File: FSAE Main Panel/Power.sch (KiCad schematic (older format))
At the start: 9 parts, among them Q301 Q_PMOS_GSD, U302 LP2985-3.3

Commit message: Added power regulator for LEDs, further GPIO considerations
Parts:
- added C?: 10uF, symbol CP1
- added C?: 100uF, symbol CP1
- added U?: LM1085-5.0, symbol LM1085-5.0
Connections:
- net labels added: DWC_+5V, LED_+5V
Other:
- note added: "LED Power"
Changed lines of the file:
@@
 	8050 4600 8200 4600
 Wire Wire Line
-	8200 4450 8200 4600
-Wire Wire Line
-	8200 4600 8200 5050
+	8200 4450 8200 5050
 Wire Wire Line
 	8200 5850 8200 5350
@@
 	6400 5200 6400 4600
 Wire Wire Line
-	6400 4600 7000 4600
-Wire Wire Line
-	7000 4600 7250 4600
-Wire Wire Line
-	6200 4450 6200 4600
-Wire Wire Line
-	6200 4600 6200 5200
+	6400 4600 7250 4600
+Wire Wire Line
+	6200 4450 6200 5200
 Text Notes 600  850  0    60   ~ 0
 Peak total draw for low power LEDs is 1.2A at 5V\nPeak total draw for high power LEDs is \nPeak total draw for alarm cluster is 800mA at 5V
@@
 	6000 4600 6000 4900
 Wire Wire Line
-	3950 5850 4600 5850
-Wire Wire Line
-	4600 5850 5200 5850
-Wire Wire Line
-	5200 5850 6700 5850
-Wire Wire Line
-	6700 5850 7000 5850
-Wire Wire Line
-	7000 5850 7650 5850
-Wire Wire Line
-	7650 5850 8200 5850
+	3950 5850 8200 5850
 $Comp
 L GND #PWR302
@@
 $EndComp
 Wire Wire Line
-	5150 4600 5200 4600
-Wire Wire Line
-	5200 4600 6000 4600
-Wire Wire Line
-	6000 4600 6200 4600
+	5150 4600 6200 4600
 Wire Wire Line
 	4600 5050 4600 5850
@@
 $EndComp
 Wire Wire Line
-	3850 4600 3950 4600
-Wire Wire Line
-	3950 4600 4050 4600
+	3850 4600 4050 4600
 Wire Wire Line
 	3950 4600 3950 5050
@@
 	1    0    0    -1
 $EndComp
+$Comp
+L +12V #PWR?
+U 1 1 5C034AE4
+P 4250 2550
+F 0 "#PWR?" H 4250 2400 50  0001 C CNN
+F 1 "+12V" H 4250 2690 50  0000 C CNN
+F 2 "" H 4250 2550 50  0001 C CNN
+F 3 "" H 4250 2550 50  0001 C CNN
+	1    4250 2550
+	1    0    0    -1
+$EndComp
+$Comp
+L LM1085-5.0 U?
+U 1 1 5C0353B0
+P 5100 2750
+F 0 "U?" H 4950 2875 50  0000 C CNN
+F 1 "LM1085-5.0" H 5100 2875 50  0000 L CNN
+F 2 "" H 5100 3000 50  0001 C CIN
+F 3 "" H 5100 2750 50  0001 C CNN
+	1    5100 2750
+	1    0    0    -1
+$EndComp
+Wire Wire Line
+	4250 2550 4250 2750
+Wire Wire Line
+	4250 2750 4800 2750
+$Comp
+L GND #PWR?
+U 1 1 5C03578E
+P 5100 3350
+F 0 "#PWR?" H 5100 3100 50  0001 C CNN
+F 1 "GND" H 5100 3200 50  0000 C CNN
+F 2 "" H 5100 3350 50  0001 C CNN
+F 3 "" H 5100 3350 50  0001 C CNN
+	1    5100 3350
+	1    0    0    -1
+$EndComp
+Wire Wire Line
+	5100 3050 5100 3350
+$Comp
+L CP1 C?
+U 1 1 5C036676
+P 4550 3050
+F 0 "C?" H 4575 3150 50  0000 L CNN
+F 1 "10uF" H 4575 2950 50  0000 L CNN
+F 2 "" H 4550 3050 50  0001 C CNN
+F 3 "" H 4550 3050 50  0001 C CNN
+	1    4550 3050
+	1    0    0    -1
+$EndComp
+$Comp
+L CP1 C?
+U 1 1 5C0366B5
+P 5650 3050
+F 0 "C?" H 5675 3150 50  0000 L CNN
+F 1 "100uF" H 5675 2950 50  0000 L CNN
+F 2 "" H 5650 3050 50  0001 C CNN
+F 3 "" H 5650 3050 50  0001 C CNN
+	1    5650 3050
+	1    0    0    -1
+$EndComp
+Wire Wire Line
+	4550 2900 4550 2750
+Connection ~ 4550 2750
+Wire Wire Line
+	4550 3200 4550 3300
+Wire Wire Line
+	4550 3300 5650 3300
+Connection ~ 5100 3300
+Wire Wire Line
+	5650 2900 5650 2750
+Wire Wire Line
+	5400 2750 6000 2750
+Wire Wire Line
+	5650 3300 5650 3200
+Text GLabel 6000 2750 2    60   Input ~ 0
+LED_+5V
+Text GLabel 6000 2550 2    60   Input ~ 0
+DWC_+5V
+Connection ~ 5650 2750
+Wire Wire Line
+	6000 2550 5850 2550
+Wire Wire Line
+	5850 2550 5850 2750
+Connection ~ 5850 2750
+Wire Notes Line
+	4100 3600 4100 2250
+Wire Notes Line
+	4100 2250 6550 2250
+Wire Notes Line
+	6550 2250 6550 3600
+Wire Notes Line
+	6550 3600 4100 3600
+Text Notes 5050 2400 0    60   ~ 0
+LED Power
 $EndSCHEMATC

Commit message: Updated to KiCad 5
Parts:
- C301, C303: renamed from C?; symbol C -> Device:C
- C302, C306: renamed from C?; symbol CP1 -> Device:CP1
- C304, C305: symbol C -> Device:C
- D301: symbol D -> Device:D
- L301: symbol Ferrite_Bead -> Device:Ferrite_Bead
- Q301: symbol Q_PMOS_GSD -> Device:Q_PMOS_GSD
- U301: renamed from U?; symbol ZLDO1117-5V -> zldo1117-5v:ZLDO1117-5V
- U302: symbol LP2985-3.3 -> regul:LP2985-3.3
- U303: renamed from U?; symbol LM1085-5.0 -> regul:LM1085-5.0
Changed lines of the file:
@@
-EESchema Schematic File Version 2
-LIBS:power
-LIBS:device
-LIBS:switches
-LIBS:relays
-LIBS:motors
-LIBS:transistors
-LIBS:conn
-LIBS:linear
-LIBS:regul
-LIBS:74xx
-LIBS:cmos4000
-LIBS:adc-dac
-LIBS:memory
-LIBS:xilinx
-LIBS:microcontrollers
-LIBS:dsp
-LIBS:microchip
-LIBS:analog_switches
-LIBS:motorola
-LIBS:texas
-LIBS:intel
-LIBS:audio
-LIBS:interface
-LIBS:digital-audio
-LIBS:philips
-LIBS:display
-LIBS:cypress
-LIBS:siliconi
-LIBS:opto
-LIBS:atmel
-LIBS:contrib
-LIBS:valves
-LIBS:TI_Additions
-LIBS:KingBright_Addition
-LIBS:lm2734
-LIBS:prtr5v0u2x
-LIBS:samd21g18a-au
-LIBS:zldo1117-5v
-LIBS:cortex_debug
+EESchema Schematic File Version 4
 LIBS:FSAE Main Panel-cache
-EELAYER 25 0
+EELAYER 26 0
 EELAYER END
 $Descr A4 11693 8268
@@
 $EndDescr
 $Comp
-L +12V #PWR301
+L power:+12V #PWR301
 U 1 1 5BD92350
 P 2800 4100
@@
 $EndComp
 $Comp
-L D D301
+L Device:D D301
 U 1 1 5BD92356
 P 3100 4600
@@
 $EndComp
 $Comp
-L Ferrite_Bead L301
+L Device:Ferrite_Bead L301
 U 1 1 5BD9235D
 P 3700 4600
@@
 $EndComp
 $Comp
-L +5V #PWR303
+L power:+5V #PWR304
 U 1 1 5BD923A9
 P 6200 4450
-F 0 "#PWR303" H 6200 4300 50  0001 C CNN
+F 0 "#PWR304" H 6200 4300 50  0001 C CNN
 F 1 "+5V" H 6200 4590 50  0000 C CNN
 F 2 "" H 6200 4450 50  0001 C CNN
@@
 $EndComp
 $Comp
-L LP2985-3.3 U302
+L regul:LP2985-3.3 U302
 U 1 1 5BD923AF
 P 7650 4700
@@
 $EndComp
 $Comp
-L C C304
+L Device:C C304
 U 1 1 5BD923BD
 P 7000 5200
@@
 	7000 5850 7000 5350
 $Comp
-L C C305
+L Device:C C305
 U 1 1 5BD92405
 P 8200 5200
@@
 Connection ~ 7650 5850
 $Comp
-L +3V3 #PWR304
+L power:+3V3 #PWR306
 U 1 1 5BD92411
 P 8200 4450
-F 0 "#PWR304" H 8200 4300 50  0001 C CNN
+F 0 "#PWR306" H 8200 4300 50  0001 C CNN
 F 1 "+3V3" H 8200 4590 50  0000 C CNN
 F 2 "" H 8200 4450 50  0001 C CNN
@@
 Connection ~ 8200 4600
 $Comp
-L Q_PMOS_GSD Q301
+L Device:Q_PMOS_GSD Q301
 U 1 1 5BD96D6D
 P 6000 5100
@@
 	3950 5850 8200 5850
 $Comp
-L GND #PWR302
+L power:GND #PWR305
 U 1 1 5BD92372
 P 6700 5950
-F 0 "#PWR302" H 6700 5700 50  0001 C CNN
+F 0 "#PWR305" H 6700 5700 50  0001 C CNN
 F 1 "GND" H 6700 5800 50  0000 C CNN
 F 2 "" H 6700 5950 50  0001 C CNN
@@
 Connection ~ 6700 5850
 $Comp
-L C C?
+L Device:C C301
 U 1 1 5BFABDFE
 P 3950 5200
-F 0 "C?" H 3975 5300 50  0000 L CNN
+F 0 "C301" H 3975 5300 50  0000 L CNN
 F 1 "4.7uF" H 3975 5100 50  0000 L CNN
 F 2 "" H 3988 5050 50  0001 C CNN
@@
 Connection ~ 3950 4600
 $Comp
-L C C?
+L Device:C C303
 U 1 1 5BFAC037
 P 5200 5200
-F 0 "C?" H 5225 5300 50  0000 L CNN
+F 0 "C303" H 5225 5300 50  0000 L CNN
 F 1 "4.7uF" H 5225 5100 50  0000 L CNN
 F 2 "" H 5238 5050 50  0001 C CNN
@@
 MCU Power
 $Comp
-L ZLDO1117-5V U?
+L zldo1117-5v:ZLDO1117-5V U301
 U 1 1 5BFDDF95
 P 4600 4600
-F 0 "U?" H 4700 4300 60  0000 C CNN
+F 0 "U301" H 4700 4300 60  0000 C CNN
 F 1 "ZLDO1117-5V" H 4600 4800 60  0000 C CNN
 F 2 "" H 4600 4600 60  0001 C CNN
@@
 $EndComp
 $Comp
-L +12V #PWR?
+L power:+12V #PWR302
 U 1 1 5C034AE4
 P 4250 2550
-F 0 "#PWR?" H 4250 2400 50  0001 C CNN
+F 0 "#PWR302" H 4250 2400 50  0001 C CNN
 F 1 "+12V" H 4250 2690 50  0000 C CNN
 F 2 "" H 4250 2550 50  0001 C CNN
@@
 $EndComp
 $Comp
-L LM1085-5.0 U?
+L regul:LM1085-5.0 U303
 U 1 1 5C0353B0
 P 5100 2750
-F 0 "U?" H 4950 2875 50  0000 C CNN
+F 0 "U303" H 4950 2875 50  0000 C CNN
 F 1 "LM1085-5.0" H 5100 2875 50  0000 L CNN
 F 2 "" H 5100 3000 50  0001 C CIN
@@
 	4250 2750 4800 2750
 $Comp
-L GND #PWR?
+L power:GND #PWR303
 U 1 1 5C03578E
 P 5100 3350
-F 0 "#PWR?" H 5100 3100 50  0001 C CNN
+F 0 "#PWR303" H 5100 3100 50  0001 C CNN
 F 1 "GND" H 5100 3200 50  0000 C CNN
 F 2 "" H 5100 3350 50  0001 C CNN
@@
 	5100 3050 5100 3350
 $Comp
-L CP1 C?
+L Device:CP1 C302
 U 1 1 5C036676
 P 4550 3050
-F 0 "C?" H 4575 3150 50  0000 L CNN
+F 0 "C302" H 4575 3150 50  0000 L CNN
 F 1 "10uF" H 4575 2950 50  0000 L CNN
 F 2 "" H 4550 3050 50  0001 C CNN
@@
 $EndComp
 $Comp
-L CP1 C?
+L Device:CP1 C306
 U 1 1 5C0366B5
 P 5650 3050
-F 0 "C?" H 5675 3150 50  0000 L CNN
+F 0 "C306" H 5675 3150 50  0000 L CNN
 F 1 "100uF" H 5675 2950 50  0000 L CNN
 F 2 "" H 5650 3050 50  0001 C CNN

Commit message: Updated Footprint Association
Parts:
- C301: footprint (none) -> Capacitors_SMD:C_1206; Description (none) -> Ceramic 4.7uF 25V X5R 1206
- C302: footprint (none) -> Capacitors_SMD:C_1206; symbol Device:CP1 -> Device:C; Description (none) -> Ceramic 10uF 25V X5R 1206
- C303: footprint (none) -> Capacitors_SMD:C_1206; Description (none) -> Ceramic 4.7uF 10V X5R 1206
- C304: footprint (none) -> Capacitors_SMD:C_1206; Description (none) -> Ceramic 47uF 10V X5R 1206
- C305: footprint (none) -> Capacitors_SMD:C_1206; Description (none) -> 4.7uF 10V X5R 1206
- C306: footprint (none) -> Capacitors_Tantalum_SMD:CP_Tantalum_Case-D_EIA-7343-31_Reflow; Description (none) -> Tantalum 100uF 10V 2917
- D301: value D -> BYS10-45-E3/TR; footprint (none) -> Diodes_SMD:D_SMA; Description (none) -> Schottky Diode 45V 1.5A DO214AC
- L301: value Ferrite_Bead -> 742792310 Ferrite Bead; footprint (none) -> Inductors_SMD:L_1210; Description (none) -> 30 Ohm Ferrite Bead 1210
- Q301: value Q_PMOS_GSD -> IRLML6402TRPBF; footprint (none) -> TO_SOT_Packages_SMD:SOT-23; Description (none) -> P-Channel MOSFET SOT-23
- U301: footprint (none) -> TO_SOT_Packages_SMD:TO-252-2
- U303: footprint (none) -> TO_SOT_Packages_SMD:TO-263-3_TabPin2; Description (none) -> Linear Regulator 5V 3A TO263
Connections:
- wire segments 35 -> 51
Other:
- note added: "Gate - 3\nSource - 2\nDrain - 1"
- moved on the sheet: D301, L301
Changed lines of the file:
@@
 $EndDescr
 $Comp
-L power:+12V #PWR301
+L power:+12V #PWR0301
 U 1 1 5BD92350
 P 2800 4100
-F 0 "#PWR301" H 2800 3950 50  0001 C CNN
+F 0 "#PWR0301" H 2800 3950 50  0001 C CNN
 F 1 "+12V" H 2800 4240 50  0000 C CNN
 F 2 "" H 2800 4100 50  0001 C CNN
@@
 L Device:D D301
 U 1 1 5BD92356
-P 3100 4600
-F 0 "D301" H 3100 4700 50  0000 C CNN
-F 1 "D" H 3100 4500 50  0000 C CNN
-F 2 "" H 3100 4600 50  0001 C CNN
-F 3 "" H 3100 4600 50  0001 C CNN
-	1    3100 4600
-	-1   0    0    1
+P 3200 4600
+F 0 "D301" H 3200 4700 50  0000 C CNN
+F 1 "BYS10-45-E3/TR" H 3200 4500 39  0000 C CNN
+F 2 "Diodes_SMD:D_SMA" H 3200 4600 50  0001 C CNN
+F 3 "" H 3200 4600 50  0001 C CNN
+F 4 "Schottky Diode 45V 1.5A DO214AC" H 3200 4600 50  0001 C CNN "Description"
+	1    3200 4600
+	-1   0    0    -1
 $EndComp
 $Comp
 L Device:Ferrite_Bead L301
 U 1 1 5BD9235D
-P 3700 4600
-F 0 "L301" V 3550 4625 50  0000 C CNN
-F 1 "Ferrite_Bead" V 3850 4600 50  0000 C CNN
-F 2 "" V 3630 4600 50  0001 C CNN
-F 3 "" H 3700 4600 50  0001 C CNN
-	1    3700 4600
-	0    1    1    0
-$EndComp
-$Comp
-L power:+5V #PWR304
+P 3750 4600
+F 0 "L301" V 3600 4625 50  0000 C CNN
+F 1 "742792310 Ferrite Bead" V 3900 4600 39  0000 C CNN
+F 2 "Inductors_SMD:L_1210" V 3680 4600 50  0001 C CNN
+F 3 "" H 3750 4600 50  0001 C CNN
+F 4 "30 Ohm Ferrite Bead 1210" V 3750 4600 50  0001 C CNN "Description"
+	1    3750 4600
+	0    1    -1   0
+$EndComp
+$Comp
+L power:+5V #PWR0304
 U 1 1 5BD923A9
 P 6200 4450
-F 0 "#PWR304" H 6200 4300 50  0001 C CNN
+F 0 "#PWR0304" H 6200 4300 50  0001 C CNN
 F 1 "+5V" H 6200 4590 50  0000 C CNN
 F 2 "" H 6200 4450 50  0001 C CNN
@@
 F 0 "C304" H 7025 5300 50  0000 L CNN
 F 1 "47uF" H 7025 5100 50  0000 L CNN
-F 2 "" H 7038 5050 50  0001 C CNN
+F 2 "Capacitors_SMD:C_1206" H 7038 5050 50  0001 C CNN
 F 3 "" H 7000 5200 50  0001 C CNN
+F 4 "Ceramic 47uF 10V X5R 1206" H 7000 5200 50  0001 C CNN "Description"
 	1    7000 5200
 	1    0    0    -1
 $EndComp
 Wire Wire Line
-	2800 4600 2950 4600
-Wire Wire Line
-	3250 4600 3550 4600
+	3350 4600 3600 4600
 Connection ~ 7000 4600
 Wire Wire Line
@@
 F 0 "C305" H 8225 5300 50  0000 L CNN
 F 1 "4.7uF" H 8225 5100 50  0000 L CNN
-F 2 "" H 8238 5050 50  0001 C CNN
+F 2 "Capacitors_SMD:C_1206" H 8238 5050 50  0001 C CNN
 F 3 "" H 8200 5200 50  0001 C CNN
+F 4 "4.7uF 10V X5R 1206" H 8200 5200 50  0001 C CNN "Description"
 	1    8200 5200
 	1    0    0    -1
@@
 	8050 4600 8200 4600
 Wire Wire Line
-	8200 4450 8200 5050
+	8200 4450 8200 4600
 Wire Wire Line
 	8200 5850 8200 5350
 Connection ~ 7650 5850
 $Comp
-L power:+3V3 #PWR306
+L power:+3V3 #PWR0306
 U 1 1 5BD92411
 P 8200 4450
-F 0 "#PWR306" H 8200 4300 50  0001 C CNN
+F 0 "#PWR0306" H 8200 4300 50  0001 C CNN
 F 1 "+3V3" H 8200 4590 50  0000 C CNN
 F 2 "" H 8200 4450 50  0001 C CNN
@@
 P 6000 5100
 F 0 "Q301" H 6200 5150 50  0000 L CNN
-F 1 "Q_PMOS_GSD" H 6200 5050 50  0000 L CNN
-F 2 "" H 6200 5200 50  0001 C CNN
+F 1 "IRLML6402TRPBF" H 6200 5050 39  0000 L CNN
+F 2 "TO_SOT_Packages_SMD:SOT-23" H 6200 5200 50  0001 C CNN
 F 3 "" H 6000 5100 50  0001 C CNN
+F 4 "P-Channel MOSFET SOT-23" H 6000 5100 50  0001 C CNN "Description"
 	1    6000 5100
-	0    1    1    0
+	0    -1   1    0
 $EndComp
 Text GLabel 5750 5200 0    39   Input ~ 0
@@
 	6400 5200 6400 4600
 Wire Wire Line
-	6400 4600 7250 4600
-Wire Wire Line
-	6200 4450 6200 5200
+	6400 4600 7000 4600
+Wire Wire Line
+	6200 4450 6200 4600
 Text Notes 600  850  0    60   ~ 0
 Peak total draw for low power LEDs is 1.2A at 5V\nPeak total draw for high power LEDs is \nPeak total draw for alarm cluster is 800mA at 5V
@@
 	6000 4600 6000 4900
 Wire Wire Line
-	3950 5850 8200 5850
-$Comp
-L power:GND #PWR305
+	3950 5850 4600 5850
+$Comp
+L power:GND #PWR0305
 U 1 1 5BD92372
 P 6700 5950
-F 0 "#PWR305" H 6700 5700 50  0001 C CNN
+F 0 "#PWR0305" H 6700 5700 50  0001 C CNN
 F 1 "GND" H 6700 5800 50  0000 C CNN
 F 2 "" H 6700 5950 50  0001 C CNN
@@
 $EndComp
 Wire Wire Line
-	5150 4600 6200 4600
+	5150 4600 5200 4600
 Wire Wire Line
 	4600 5050 4600 5850
@@
 F 0 "C301" H 3975 5300 50  0000 L CNN
 F 1 "4.7uF" H 3975 5100 50  0000 L CNN
-F 2 "" H 3988 5050 50  0001 C CNN
+F 2 "Capacitors_SMD:C_1206" H 3988 5050 50  0001 C CNN
 F 3 "" H 3950 5200 50  0001 C CNN
+F 4 "Ceramic 4.7uF 25V X5R 1206" H 3950 5200 50  0001 C CNN "Description"
 	1    3950 5200
 	1    0    0    -1
 $EndComp
 Wire Wire Line
-	3850 4600 4050 4600
+	3900 4600 3950 4600
 Wire Wire Line
 	3950 4600 3950 5050
@@
 F 0 "C303" H 5225 5300 50  0000 L CNN
 F 1 "4.7uF" H 5225 5100 50  0000 L CNN
-F 2 "" H 5238 5050 50  0001 C CNN
+F 2 "Capacitors_SMD:C_1206" H 5238 5050 50  0001 C CNN
 F 3 "" H 5200 5200 50  0001 C CNN
+F 4 "Ceramic 4.7uF 10V X5R 1206" H 5200 5200 50  0001 C CNN "Description"
 	1    5200 5200
 	1    0    0    -1
@@
 F 0 "U301" H 4700 4300 60  0000 C CNN
 F 1 "ZLDO1117-5V" H 4600 4800 60  0000 C CNN
-F 2 "" H 4600 4600 60  0001 C CNN
+F 2 "TO_SOT_Packages_SMD:TO-252-2" H 4600 4600 60  0001 C CNN
 F 3 "" H 4600 4600 60  0001 C CNN
 	1    4600 4600
@@
 $EndComp
 $Comp
-L power:+12V #PWR302
+L power:+12V #PWR0302
 U 1 1 5C034AE4
-P 4250 2550
-F 0 "#PWR302" H 4250 2400 50  0001 C CNN
-F 1 "+12V" H 4250 2690 50  0000 C CNN
-F 2 "" H 4250 2550 50  0001 C CNN
-F 3 "" H 4250 2550 50  0001 C CNN
-	1    4250 2550
+P 4150 2550
+F 0 "#PWR0302" H 4150 2400 50  0001 C CNN
+F 1 "+12V" H 4150 2690 50  0000 C CNN
+F 2 "" H 4150 2550 50  0001 C CNN
+F 3 "" H 4150 2550 50  0001 C CNN
+	1    4150 2550
 	1    0    0    -1
 $EndComp
@@
 F 0 "U303" H 4950 2875 50  0000 C CNN
 F 1 "LM1085-5.0" H 5100 2875 50  0000 L CNN
-F 2 "" H 5100 3000 50  0001 C CIN
+F 2 "TO_SOT_Packages_SMD:TO-263-3_TabPin2" H 5100 3000 50  0001 C CIN
 F 3 "" H 5100 2750 50  0001 C CNN
+F 4 "Linear Regulator 5V 3A TO263" H 5100 2750 50  0001 C CNN "Description"
 	1    5100 2750
 	1    0    0    -1
 $EndComp
 Wire Wire Line
-	4250 2550 4250 2750
-Wire Wire Line
-	4250 2750 4800 2750
-$Comp
-L power:GND #PWR303
+	4150 2550 4150 2750
+Wire Wire Line
+	4150 2750 4500 2750
+$Comp
+L power:GND #PWR0303
 U 1 1 5C03578E
 P 5100 3350
-F 0 "#PWR303" H 5100 3100 50  0001 C CNN
+F 0 "#PWR0303" H 5100 3100 50  0001 C CNN
 F 1 "GND" H 5100 3200 50  0000 C CNN
 F 2 "" H 5100 3350 50  0001 C CNN
@@
 $EndComp
 Wire Wire Line
-	5100 3050 5100 3350
-$Comp
-L Device:CP1 C302
+	5100 3050 5100 3300
+$Comp
+L Device:C C302
 U 1 1 5C036676
-P 4550 3050
-F 0 "C302" H 4575 3150 50  0000 L CNN
-F 1 "10uF" H 4575 2950 50  0000 L CNN
-F 2 "" H 4550 3050 50  0001 C CNN
-F 3 "" H 4550 3050 50  0001 C CNN
-	1    4550 3050
+P 4500 3050
+F 0 "C302" H 4525 3150 50  0000 L CNN
+F 1 "10uF" H 4525 2950 50  0000 L CNN
+F 2 "Capacitors_SMD:C_1206" H 4500 3050 50  0001 C CNN
+F 3 "" H 4500 3050 50  0001 C CNN
+F 4 "Ceramic 10uF 25V X5R 1206" H 4500 3050 50  0001 C CNN "Description"
+	1    4500 3050
 	1    0    0    -1
 $EndComp
@@
 F 0 "C306" H 5675 3150 50  0000 L CNN
 F 1 "100uF" H 5675 2950 50  0000 L CNN
-F 2 "" H 5650 3050 50  0001 C CNN
+F 2 "Capacitors_Tantalum_SMD:CP_Tantalum_Case-D_EIA-7343-31_Reflow" H 5650 3050 50  0001 C CNN
 F 3 "" H 5650 3050 50  0001 C CNN
+F 4 "Tantalum 100uF 10V 2917" H 5650 3050 50  0001 C CNN "Description"
 	1    5650 3050
 	1    0    0    -1
 $EndComp
 Wire Wire Line
-	4550 2900 4550 2750
-Connection ~ 4550 2750
-Wire Wire Line
-	4550 3200 4550 3300
-Wire Wire Line
-	4550 3300 5650 3300
+	4500 2900 4500 2750
+Connection ~ 4500 2750
+Wire Wire Line
+	4500 3200 4500 3300
+Wire Wire Line
+	4500 3300 5100 3300
 Connection ~ 5100 3300
 Wire Wire Line
 	5650 2900 5650 2750
 Wire Wire Line
-	5400 2750 6000 2750
+	5400 2750 5650 2750
 Wire Wire Line
 	5650 3300 5650 3200
@@
 Connection ~ 5850 2750
 Wire Notes Line
-	4100 3600 4100 2250
-Wire Notes Line
-	4100 2250 6550 2250
+	4000 3600 4000 2250
+Wire Notes Line
+	4000 2250 6550 2250
 Wire Notes Line
 	6550 2250 6550 3600
 Wire Notes Line
-	6550 3600 4100 3600
+	6550 3600 4000 3600
 Text Notes 5050 2400 0    60   ~ 0
 LED Power
+Wire Wire Line
+	7000 4600 7250 4600
+Wire Wire Line
+	7000 5850 7650 5850
+Wire Wire Line
+	7650 5850 8200 5850
+Wire Wire Line
+	8200 4600 8200 5050
+Wire Wire Line
+	6200 4600 6200 5200
+Wire Wire Line
+	6000 4600 6200 4600
+Wire Wire Line
+	6700 5850 7000 5850
+Wire Wire Line
+	4600 5850 5200 5850
+Wire Wire Line
+	3950 4600 4050 4600
+Wire Wire Line
+	5200 4600 6000 4600
+Wire Wire Line
+	5200 5850 6700 5850
+Wire Wire Line
+	4500 2750 4800 2750
+Wire Wire Line
+	5100 3300 5100 3350
+Wire Wire Line
+	5100 3300 5650 3300
+Wire Wire Line
+	5650 2750 5850 2750
+Wire Wire Line
+	5850 2750 6000 2750
+Connection ~ 6200 5200
+Text Notes 6200 5500 0    50   ~ 0
+Gate - 3\nSource - 2\nDrain - 1
+Wire Wire Line
+	2800 4600 3050 4600
 $EndSCHEMATC

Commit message: New footprints, finished associating footprints
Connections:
- net labels added: CAN_V+
- net labels removed: +12V
- wire segments 51 -> 49
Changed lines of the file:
@@
 $EndDescr
-$Comp
-L power:+12V #PWR0301
-U 1 1 5BD92350
-P 2800 4100
-F 0 "#PWR0301" H 2800 3950 50  0001 C CNN
-F 1 "+12V" H 2800 4240 50  0000 C CNN
-F 2 "" H 2800 4100 50  0001 C CNN
-F 3 "" H 2800 4100 50  0001 C CNN
-	1    2800 4100
-	1    0    0    -1
-$EndComp
 $Comp
 L Device:D D301
@@
 Text Notes 600  850  0    60   ~ 0
 Peak total draw for low power LEDs is 1.2A at 5V\nPeak total draw for high power LEDs is \nPeak total draw for alarm cluster is 800mA at 5V
-Wire Wire Line
-	2800 4100 2800 4600
 Connection ~ 6200 4600
 Connection ~ 6000 4600
@@
 $EndComp
 $Comp
-L power:+12V #PWR0302
-U 1 1 5C034AE4
-P 4150 2550
-F 0 "#PWR0302" H 4150 2400 50  0001 C CNN
-F 1 "+12V" H 4150 2690 50  0000 C CNN
-F 2 "" H 4150 2550 50  0001 C CNN
-F 3 "" H 4150 2550 50  0001 C CNN
-	1    4150 2550
-	1    0    0    -1
-$EndComp
-$Comp
 L regul:LM1085-5.0 U303
 U 1 1 5C0353B0
@@
 $EndComp
 Wire Wire Line
-	4150 2550 4150 2750
-Wire Wire Line
-	4150 2750 4500 2750
+	4400 2750 4500 2750
 $Comp
 L power:GND #PWR0303
@@
 Text Notes 6200 5500 0    50   ~ 0
 Gate - 3\nSource - 2\nDrain - 1
-Wire Wire Line
-	2800 4600 3050 4600
+Text GLabel 4400 2750 0    50   Input ~ 0
+CAN_V+
+Text GLabel 2900 4600 0    50   Input ~ 0
+CAN_V+
+Wire Wire Line
+	3050 4600 2900 4600
 $EndSCHEMATC

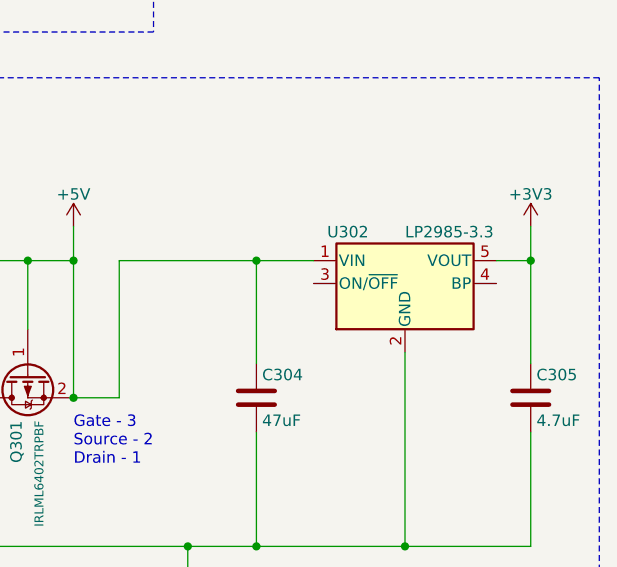
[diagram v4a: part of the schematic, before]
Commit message: Edited footprints, started PCB layout
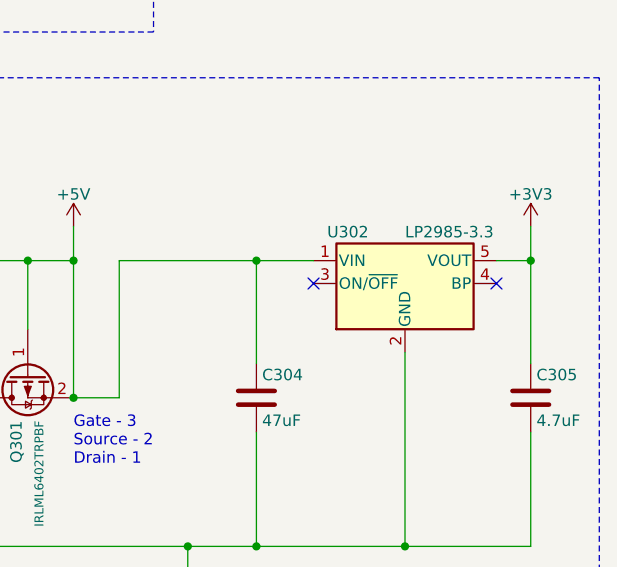
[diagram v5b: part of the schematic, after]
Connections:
- no-connect marks 0 -> 2
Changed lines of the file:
@@
 Wire Wire Line
 	3050 4600 2900 4600
+NoConn ~ 8050 4700
+NoConn ~ 7250 4700
 $EndSCHEMATC
